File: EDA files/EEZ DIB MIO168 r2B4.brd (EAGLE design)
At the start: 146 x 95 mm, 266 parts, among them IC1 M24C32-WMN6P, IC10 OPA2196IDR, IC11 DAC7760IPWPR, IC12 DAC7760IPWPR, IC13 OPA376AIDBVR, IC14 DAC7563TDGSR, IC15 OPA2196IDR, IC16 BTS3408G, IC17 BTS3408G, IC18 BTS3408G, IC19 BTS3408G, IC2 Si8641BB-B-IS1, IC20 TL431B, IC21 74HC126PW,118, IC22 74HC126PW,118, IC3 Si8641BB-B-IS1, IC4 LP2985-33DBVR, IC5 L78L15, IC6 SN6505BDBVT, IC7 L79L15, IC8 STM32F446ZCT6, J1 4907, J2 N.C., K1 TQ2SS-L2-5V-X, K2 TQ2SS-L2-5V-X, Q1 2N7002PS,115, Q10 MMBT5551, Q11 2N7002, Q2 2N7002PS,115, Q3 2N7002PS,115, Q4 2N7002PS,115, Q5 2N7002PS,115, Q6 BSS84P, Q7 MMBT5401, Q8 BSS84P, Q9 MMBT5551, X1 77317-104-28LF, X2 N.C., X3 691327310016, X4 691322310008, X5 DS1014-10RF1B, X6 DS1014-10RF1B, X7 DS1023-2*14S21, X8 DS1023-2*14S21, Y1 LF XTAL026392

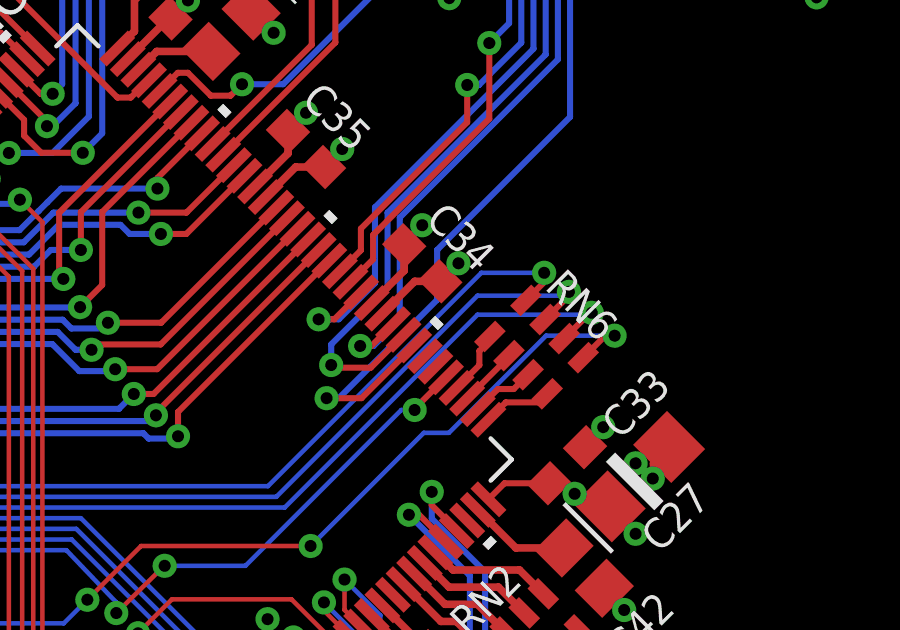
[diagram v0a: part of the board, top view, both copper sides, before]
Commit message: PCB ID added
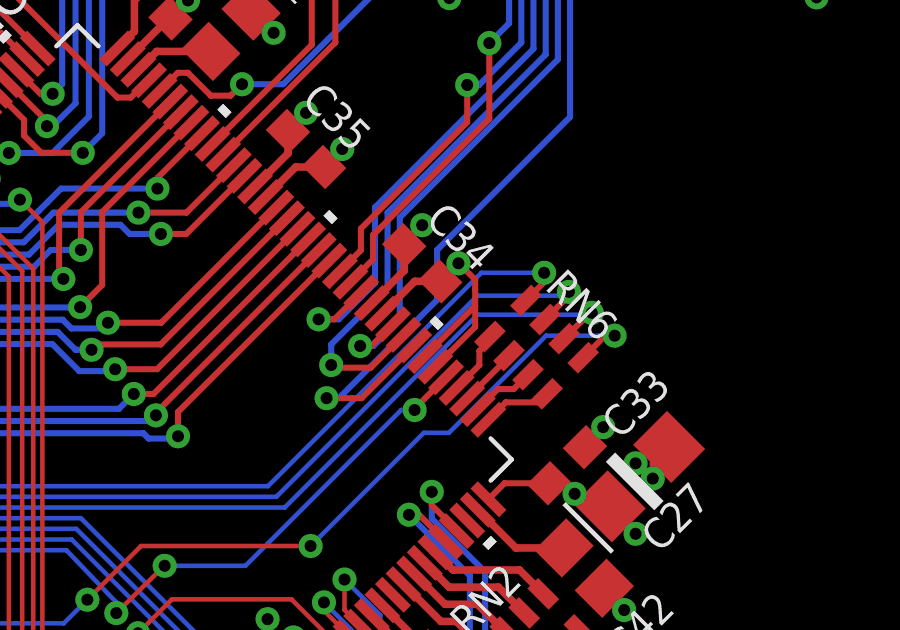
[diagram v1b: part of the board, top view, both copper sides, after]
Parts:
- IC9: value (none) -> N.C.
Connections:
- net GND: now also IC8.78, IC8.79
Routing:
- net GND: track 213.8 -> 220.5 mm
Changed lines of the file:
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@@
 <grid distance="0.5" unitdist="mil" unit="mil" style="lines" multiple="10" display="no" altdistance="2.5" altunitdist="mil" altunit="mil"/>
 <layers>
-<layer number="1" name="Top" color="3" fill="1" visible="no" active="yes"/>
+<layer number="1" name="Top" color="3" fill="1" visible="yes" active="yes"/>
 <layer number="2" name="L2" color="2" fill="1" visible="no" active="yes"/>
 <layer number="3" name="Route3" color="4" fill="3" visible="no" active="no"/>
@@
 <layer number="13" name="Route13" color="4" fill="5" visible="no" active="no"/>
 <layer number="14" name="Route14" color="1" fill="6" visible="no" active="no"/>
-<layer number="15" name="L3" color="6" fill="1" visible="no" active="yes"/>
-<layer number="16" name="Bottom" color="1" fill="1" visible="no" active="yes"/>
-<layer number="17" name="Pads" color="14" fill="1" visible="no" active="yes"/>
-<layer number="18" name="Vias" color="6" fill="1" visible="no" active="yes"/>
-<layer number="19" name="Unrouted" color="6" fill="1" visible="no" active="yes"/>
+<layer number="15" name="L3" color="6" fill="1" visible="yes" active="yes"/>
+<layer number="16" name="Bottom" color="1" fill="1" visible="yes" active="yes"/>
+<layer number="17" name="Pads" color="14" fill="1" visible="yes" active="yes"/>
+<layer number="18" name="Vias" color="6" fill="1" visible="yes" active="yes"/>
+<layer number="19" name="Unrouted" color="6" fill="1" visible="yes" active="yes"/>
 <layer number="20" name="Dimension" color="12" fill="1" visible="yes" active="yes"/>
 <layer number="21" name="tPlace" color="7" fill="1" visible="yes" active="yes"/>
@@
 <layer number="37" name="tTest" color="7" fill="1" visible="no" active="yes"/>
 <layer number="38" name="bTest" color="7" fill="1" visible="no" active="yes"/>
-<layer number="39" name="tKeepout" color="15" fill="1" visible="yes" active="yes"/>
+<layer number="39" name="tKeepout" color="15" fill="1" visible="no" active="yes"/>
 <layer number="40" name="bKeepout" color="5" fill="1" visible="no" active="yes"/>
 <layer number="41" name="tRestrict" color="4" fill="10" visible="no" active="yes"/>
@@
 <wire x1="143.9418" y1="75.9968" x2="143.9672" y2="75.9968" width="0.2032" layer="133"/>
 <wire x1="144.0053" y1="91.0463" x2="128.8923" y2="76.2762" width="0.2032" layer="133"/>
-<wire x1="138.3538" y1="93.6752" x2="142.3797" y2="91.6432" width="0.2032" layer="133"/>
-<wire x1="142.3797" y1="93.5863" x2="138.5316" y2="91.6432" width="0.2032" layer="133"/>
-<wire x1="125.6919" y1="84.2899" x2="127.635" y2="80.3021" width="0.2032" layer="133"/>
-<wire x1="127.6096" y1="84.2899" x2="125.7554" y2="80.3783" width="0.2032" layer="133"/>
-<wire x1="107.6071" y1="87.5411" x2="123.0884" y2="85.2932" width="0.2032" layer="133"/>
-<wire x1="123.1138" y1="87.5665" x2="107.6325" y2="85.3313" width="0.2032" layer="133"/>
-<wire x1="121.4628" y1="80.9117" x2="124.6759" y2="78.2066" width="0.2032" layer="133"/>
-<wire x1="124.7394" y1="80.8736" x2="121.5009" y2="78.2193" width="0.2032" layer="133"/>
+<wire x1="137.0076" y1="93.5101" x2="140.8811" y2="91.6178" width="0.2032" layer="133"/>
+<wire x1="140.9065" y1="93.5228" x2="137.0203" y2="91.6178" width="0.2032" layer="133"/>
+<wire x1="121.8184" y1="83.9851" x2="124.46" y2="80.8355" width="0.2032" layer="133"/>
+<wire x1="124.46" y1="83.9724" x2="121.8311" y2="80.8355" width="0.2032" layer="133"/>
+<wire x1="96.4057" y1="87.5411" x2="111.8743" y2="85.2932" width="0.2032" layer="133"/>
+<wire x1="111.8235" y1="87.5538" x2="96.4565" y2="85.2805" width="0.2032" layer="133"/>
+<wire x1="115.0112" y1="86.4616" x2="119.5578" y2="77.5208" width="0.2032" layer="133"/>
+<wire x1="119.5451" y1="86.4616" x2="115.0493" y2="77.4573" width="0.2032" layer="133"/>
+<wire x1="121.1199" y1="79.7941" x2="124.9807" y2="77.9145" width="0.2032" layer="133"/>
+<wire x1="124.9934" y1="79.7941" x2="121.1326" y2="77.9272" width="0.2032" layer="133"/>
 </plain>
 <attributes>
@@
 <element name="JP2" library="EEZ_connectors" package="ZL303-03P" value="DS1025-01-1*3P8BV1-B" x="54.9783" y="87.8078" smashed="yes">
 <attribute name="NAME" x="49.809" y="87.3793" size="0.8128" layer="25" ratio="10"/>
-<attribute name="VALUE" x="54.9783" y="87.8078" size="0.6096" layer="27" align="center"/>
+<attribute name="VALUE" x="54.9783" y="87.8078" size="0.4064" layer="27" align="center"/>
 </element>
 <element name="JP3" library="EEZ_connectors" package="ZL303-03P" value="DS1025-01-1*3P8BV1-B" x="36.576" y="87.8078" smashed="yes" rot="R180">
 <attribute name="NAME" x="32.6677" y="88.875" size="0.8128" layer="25" ratio="10" rot="R270"/>
-<attribute name="VALUE" x="36.576" y="87.8078" size="0.6096" layer="27" rot="R180" align="center"/>
+<attribute name="VALUE" x="36.576" y="87.8078" size="0.4064" layer="27" rot="R180" align="center"/>
 </element>
 <element name="JP4" library="EEZ_connectors" package="ZL303-03P" value="DS1025-01-1*3P8BV1-B" x="54.9783" y="85.6488" smashed="yes" rot="R180">
 <attribute name="NAME" x="49.8725" y="85.3981" size="0.8128" layer="25" ratio="10"/>
-<attribute name="VALUE" x="54.9783" y="85.6488" size="0.6096" layer="27" rot="R180" align="center"/>
+<attribute name="VALUE" x="54.9783" y="85.6488" size="0.4064" layer="27" rot="R180" align="center"/>
 </element>
 <element name="JP5" library="EEZ_connectors" package="ZL303-03P" value="DS1025-01-1*3P8BV1-B" x="36.576" y="85.6488" smashed="yes">
 <attribute name="NAME" x="33.4358" y="84.4546" size="0.8128" layer="25" ratio="10" rot="R90"/>
-<attribute name="VALUE" x="36.576" y="85.6488" size="0.6096" layer="27" align="center"/>
+<attribute name="VALUE" x="36.576" y="85.6488" size="0.4064" layer="27" align="center"/>
 </element>
 <element name="K1" library="EEZ_switches" package="PANASONIC_TQ2_SS" value="TQ2SS-L2-5V-X" x="47.6885" y="72.3265" smashed="yes" rot="R90">
@@
 <attribute name="VALUE" x="75.0189" y="72.0217" size="0.8128" layer="27" ratio="10" rot="R270"/>
 </element>
-<element name="IC9" library="EEZ_DIB" package="LGA8" value="" x="117.2972" y="81.9531" smashed="yes" rot="R270">
+<element name="IC9" library="EEZ_DIB" package="LGA8" value="N.C." x="117.2972" y="81.9531" smashed="yes" rot="R270">
 <attribute name="NAME" x="116.078" y="86.7791" size="1.016" layer="25" ratio="10"/>
 <attribute name="VALUE" x="117.2972" y="81.9531" size="1.016" layer="27" ratio="10" rot="R270" align="center"/>
@@
 <wire x1="130.5687" y1="75.3872" x2="130.5687" y2="75.5257" width="0.2032" layer="1"/>
 <wire x1="130.5687" y1="75.5257" x2="131.648" y2="76.605" width="0.2032" layer="1"/>
+<contactref element="IC8" pad="78"/>
+<contactref element="IC8" pad="79"/>
+<wire x1="129.752371875" y1="63.45464375" x2="131.4323" y2="65.134571875" width="0.2032" layer="1"/>
+<wire x1="131.4323" y1="65.134571875" x2="131.4323" y2="65.6844" width="0.2032" layer="1"/>
+<wire x1="131.4323" y1="65.6844" x2="131.4323" y2="66.0019" width="0.2032" layer="1"/>
+<wire x1="131.4323" y1="66.0019" x2="130.8862" y2="66.548" width="0.2032" layer="1"/>
+<wire x1="130.8862" y1="66.548" x2="130.8735" y2="66.548" width="0.2032" layer="1"/>
+<wire x1="130.105925" y1="63.101090625" x2="131.4323" y2="64.427465625" width="0.2032" layer="1"/>
+<wire x1="131.4323" y1="64.427465625" x2="131.4323" y2="65.134571875" width="0.2032" layer="1"/>
 </signal>
 <signal name="DIB_A0">
